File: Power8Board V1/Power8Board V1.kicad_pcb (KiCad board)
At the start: 6 copper layers, 217.4 x 102.2 mm, 107 parts, among them J0 XT30, J1 XT30, J10 XT60IPW-M, J2 XT30, J3 XT30, J4 XT30, J5 XT30, J6 XT30, J7 XT30, J8 Qwiic_RA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

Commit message: DRC sorted out.
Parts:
- removed the R25 at (146.2, 104.1)
- added R5: 680, Resistor_SMD:R_0603_1608Metric, F.Cu at (146.2, 104.1)
- renumbered R5 to R25
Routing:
- net Net-(U12-AIN1): vias 1 -> 0
- net Net-(U12-AIN0): vias 1 -> 0
- net +5V: vias 3 -> 2
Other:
- board size 217.4 x 102.2 mm -> 304 x 106.4 mm

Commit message: PCB before BOM creation.
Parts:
- moved J8 28.5 mm to (150.0, 54.8)
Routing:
- net +5V: track 167.7 -> 208.7 mm
- net SDA: track 127.4 -> 118.3 mm
- net SCL: track 117.4 -> 111.8 mm
- net +3.3V: track 94.5 -> 96.9 mm
- net /Current Sensing/INA240 Current Sensor 0/OUT0: track 50.7 -> 52.7 mm
- net /Current Sensing/INA240 Current Sensor 3/OUT3: track 39.6 -> 40.3 mm
- net +12V/7: vias 0 -> 5
- net +12V/6: vias 0 -> 5
- net +12V/5: vias 0 -> 5
- net +12V/4: vias 0 -> 5
- net +12V/3: vias 0 -> 5
- net +12V/2: vias 0 -> 5
- net +12V/1: vias 0 -> 5
- net +12V/0: vias 0 -> 5
- net +12V: vias 0 -> 20
- added copper zone on B.Cu, net +12V
- added copper zone on B.Cu, net +12V/0
- added copper zone on B.Cu, net +12V/1
- added copper zone on B.Cu, net +12V/2
- added copper zone on B.Cu, net +12V/3
- added copper zone on B.Cu, net +12V/4
- added copper zone on B.Cu, net +12V/5
- added copper zone on B.Cu, net +12V/6
- added copper zone on B.Cu, net +12V/7
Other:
- board size 304 x 106.4 mm -> 102 x 102 mm
- board text removed: "CHECK PINS"
- board text removed: "PIN RECEPTACLES"

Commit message: Ordered PCB.
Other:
- board text added: "Power8Board V1"
- board text added: "V1.0 9/2025 By Harry O'Hagin"
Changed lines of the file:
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@@
 			(plot_on_all_layers_selection 0x0000000_00000000)
 			(disableapertmacros no)
-			(usegerberextensions no)
+			(usegerberextensions yes)
 			(usegerberattributes yes)
 			(usegerberadvancedattributes yes)
-			(creategerberjobfile yes)
+			(creategerberjobfile no)
 			(dashed_line_dash_ratio 12.000000)
 			(dashed_line_gap_ratio 3.000000)
@@
 			(psa4output no)
 			(plotreference yes)
-			(plotvalue yes)
+			(plotvalue no)
 			(plotfptext yes)
 			(plotinvisibletext no)
 			(sketchpadsonfab no)
-			(subtractmaskfromsilk no)
+			(subtractmaskfromsilk yes)
 			(outputformat 1)
 			(mirror no)
-			(drillshape 1)
+			(drillshape 0)
 			(scaleselection 1)
-			(outputdirectory "")
+			(outputdirectory "Export/")
 		)
 	)
@@
 		(layer "Edge.Cuts")
 	)
+	(gr_text "V1.0 9/2025\nBy Harry O'Hagin"
+		(at 189 150.5 0)
+		(layer "B.SilkS")
+		(effects
+			(font
+				(size 1.5 1.5)
+				(thickness 0.3)
+				(bold yes)
+			)
+			(justify left bottom mirror)
+		)
+	)
+	(gr_text "Power8Board V1"
+		(at 114 150.5 0)
+		(layer "F.Mask")
+		(effects
+			(font
+				(size 1.5 1.5)
+				(thickness 0.3)
+				(bold yes)
+				(italic yes)
+			)
+			(justify left bottom)
+		)
+	)
 	(segment
 		(start 118.600001 137.5)
@@
 			)
 		)
+	)
+	(zone
+		(net 0)
+		(net_name "")
+		(layer "F.Cu")
+		(hatch edge 0.5)
+		(connect_pads yes
+			(clearance 0)
+		)
+		(min_thickness 0.25)
+		(filled_areas_thickness no)
+		(keepout
+			(tracks allowed)
+			(vias allowed)
+			(pads allowed)
+			(copperpour not_allowed)
+			(footprints allowed)
+		)
+		(fill
+			(thermal_gap 0.5)
+			(thermal_bridge_width 0.5)
+		)
+		(polygon
+			(pts
+				(xy 144.25 75.75) (xy 144.25 83) (xy 160.75 83) (xy 160.75 75.75)
+			)
+		)

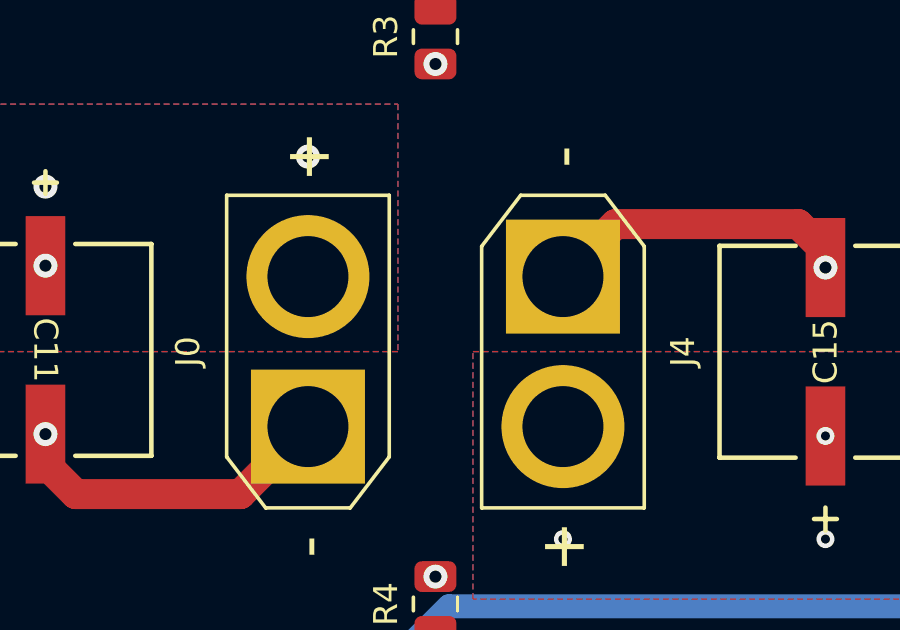
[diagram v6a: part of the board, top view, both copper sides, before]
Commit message: Added non KiCad standard components in Components folder.
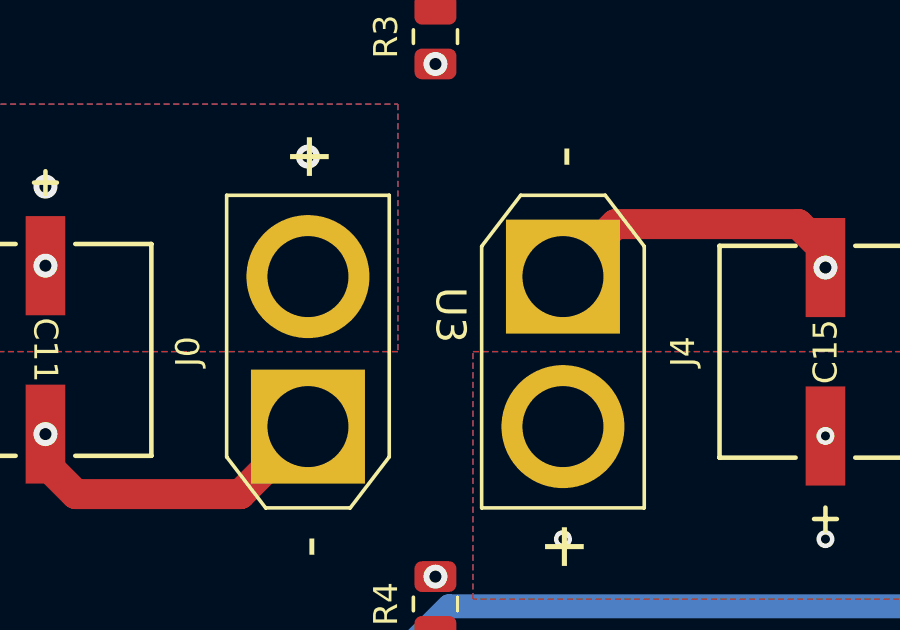
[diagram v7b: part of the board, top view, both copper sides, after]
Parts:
- U3: footprint UWS-5_10-Q48P-C:UWS-5_10-Q48P-C -> UWS-5_10-Q48:UWS-5_10-Q48
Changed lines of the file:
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@@
 		(property ki_fp_filters "Inductor_* L_* *Ferrite*")
 		(sheetname "INA240 Current Sensor 7")
-		(sheetfile "INA240 Current Sensor 7.kicad_sch")
+		(sheetfile "Current Sensors/INA240 Current Sensor 7.kicad_sch")
 		(attr smd)
 		(fp_line
@@
 		(property ki_fp_filters "C_*")
 		(sheetname "INA240 Current Sensor 7")
-		(sheetfile "INA240 Current Sensor 7.kicad_sch")
+		(sheetfile "Current Sensors/INA240 Current Sensor 7.kicad_sch")
 		(attr smd)
 		(fp_line
@@
 		(property ki_fp_filters "R_*")
 		(sheetname "INA240 Current Sensor 7")
-		(sheetfile "INA240 Current Sensor 7.kicad_sch")
+		(sheetfile "Current Sensors/INA240 Current Sensor 7.kicad_sch")
 		(attr smd)
 		(fp_line
@@
 		(property ki_fp_filters "PW0008A_N_TEX PW0008A_M PW0008A_L")
 		(sheetname "INA240 Current Sensor 7")
-		(sheetfile "INA240 Current Sensor 7.kicad_sch")
+		(sheetfile "Current Sensors/INA240 Current Sensor 7.kicad_sch")
 		(attr smd)
 		(fp_line
@@
 		)
 	)
-	(footprint "UWS-5_10-Q48P-C:UWS-5_10-Q48P-C"
+	(footprint "UWS-5_10-Q48:UWS-5_10-Q48"
 		(layer "F.Cu")
 		(at 150 136.28 -90)
 		(property "Reference" "U3"
-			(at 0.22 0 0)
+			(at 0 -0.5 -90)
 			(unlocked yes)
-			(layer "B.SilkS")
+			(layer "F.SilkS")
 			(effects
 				(font
-					(size 0.8 0.8)
-					(thickness 0.15)
+					(size 1 1)
+					(thickness 0.1)
 				)
-				(justify mirror)
 			)
 		)
@@
 			)
 		)
-		(property "Footprint" "UWS-5_10-Q48P-C:UWS-5_10-Q48P-C"
+		(property "Footprint" "UWS-5_10-Q48:UWS-5_10-Q48"
 			(at 0 0 -90)
 			(unlocked yes)
